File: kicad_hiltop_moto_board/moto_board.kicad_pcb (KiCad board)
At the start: 4 copper layers, 159.9 x 99.9 mm, 213 parts, among them J1 Conn_01x04, J2 Conn_01x04, J3 Conn_03x32_DIN41612, J4 Conn_01x04, J5 Conn_02x05_Top_Bottom, J6 Conn_01x04, J7 Conn_01x04, J8 Conn_01x04, J9 Conn_01x04, Q1 CSD18540Q5B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

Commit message: moto board 3d connector models added
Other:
- board text added: "CH.A"
- board text added: "CH.B"
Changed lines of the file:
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@@
   (general
     (thickness 1.6)
-    (drawings 44)
+    (drawings 48)
     (tracks 1841)
     (zones 0)
@@
     (0 F.Cu signal)
     (1 In1.Cu signal)
-    (2 In2.Cu signal)
+    (2 In2.Cu signal hide)
     (31 B.Cu signal)
     (32 B.Adhes user)
@@
     (pad 1 thru_hole rect (at -5.25 -2.5 270) (size 2.1 2.1) (drill 1.1) (layers *.Cu *.Mask)
       (net 114 /A1))
+    (model /home/adil/Documents/LBBC/KiCAD/kicad_hiltop_moto_board/pxc_1862068_01_SPTAF-1-4-3-5-EL_3D.stp
+      (offset (xyz -7.75 -5.5 0))
+      (scale (xyz 1 1 1))
+      (rotate (xyz 0 0 0))
+    )
   )
   (module Devtank_PCB_Lib:Phoenix_Contact_SPTAF_4_way_terminal_block (layer F.Cu)
@@
     (pad 1 thru_hole rect (at -5.25 -2.5 270) (size 2.1 2.1) (drill 1.1) (layers *.Cu *.Mask)
       (net 111 /B1))
+    (model /home/adil/Documents/LBBC/KiCAD/kicad_hiltop_moto_board/pxc_1862068_01_SPTAF-1-4-3-5-EL_3D.stp
+      (offset (xyz -7.75 -5.5 0))
+      (scale (xyz 1 1 1))
+      (rotate (xyz 0 0 0))
+    )
   )
   (module Resistor_SMD:R_1210_3225Metric (layer F.Cu)
@@
     (tags capacitor)
     (attr smd)
-    (fp_text reference C95 (at -1.96 1.91 180) (layer F.SilkS)
-      (effects (font (size 0.7 0.7) (thickness 0.15)))
+    (fp_text reference C95 (at -1.29 -0.11 270) (layer F.SilkS)
+      (effects (font (size 0.5 0.5) (thickness 0.1)))
     )
     (fp_text value 0.1uF (at 0 1.17 180) (layer F.Fab)
@@
     (tags capacitor)
     (attr smd)
-    (fp_text reference C100 (at -1.285 -1.61 270) (layer F.SilkS)
+    (fp_text reference C100 (at -2.105 0.49) (layer F.SilkS)
       (effects (font (size 0.5 0.5) (thickness 0.1)))
     )
@@
     (pad 7 thru_hole circle (at -12.7 10.16) (size 4.572 4.572) (drill 4.064) (layers *.Cu *.Mask))
     (pad 8 thru_hole circle (at -2.54 10.16) (size 4.572 4.572) (drill 4.064) (layers *.Cu *.Mask))
+    (model /home/adil/Documents/LBBC/KiCAD/kicad_hiltop_moto_board/c-0641737-01-g-3d.stp
+      (offset (xyz -7.5 -12.75 4))
+      (scale (xyz 1 1 1))
+      (rotate (xyz -90 0 0))
+    )
   )
   (module TestPoint:TestPoint_THTPad_D1.0mm_Drill0.5mm (layer F.Cu)
@@
     (descr "Through hole straight pin header, 2x03, 2.54mm pitch, double rows")
     (tags "Through hole pin header THT 2x03 2.54mm double row")
-    (fp_text reference J6 (at -0.96 -2.5) (layer F.SilkS)
+    (fp_text reference J6 (at -2.66 6.4) (layer F.SilkS)
       (effects (font (size 1 1) (thickness 0.15)))
     )
@@
     (descr "Through hole straight pin header, 2x03, 2.54mm pitch, double rows")
     (tags "Through hole pin header THT 2x03 2.54mm double row")
-    (fp_text reference J7 (at -1 -2.5) (layer F.SilkS)
+    (fp_text reference J7 (at -2.66 6.3) (layer F.SilkS)
       (effects (font (size 1 1) (thickness 0.15)))
     )
@@
     (descr "Through hole straight pin header, 2x03, 2.54mm pitch, double rows")
     (tags "Through hole pin header THT 2x03 2.54mm double row")
-    (fp_text reference J8 (at -0.96 -2.5) (layer F.SilkS)
+    (fp_text reference J8 (at -2.66 6) (layer F.SilkS)
       (effects (font (size 1 1) (thickness 0.15)))
     )
@@
     (descr "Through hole straight pin header, 2x03, 2.54mm pitch, double rows")
     (tags "Through hole pin header THT 2x03 2.54mm double row")
-    (fp_text reference J9 (at -1 -2.6) (layer F.SilkS)
+    (fp_text reference J9 (at -2.66 6.3) (layer F.SilkS)
       (effects (font (size 1 1) (thickness 0.15)))
     )
@@
     (pad 1 np_thru_hole circle (at 0 0) (size 2.7 2.7) (drill 2.7) (layers *.Cu *.Mask))
   )
+  (gr_text "CH.B\n" (at 90.9 116.2) (layer F.SilkS)
+    (effects (font (size 0.5 0.5) (thickness 0.1)))
+  )
+  (gr_text "CH.B\n" (at 78.8 116.2) (layer F.SilkS)
+    (effects (font (size 0.5 0.5) (thickness 0.1)))
+  )
+  (gr_text CH.A (at 90.8 105.2) (layer F.SilkS)
+    (effects (font (size 0.5 0.5) (thickness 0.1)))
+  )
+  (gr_text CH.A (at 78.8 105.2) (layer F.SilkS)
+    (effects (font (size 0.5 0.5) (thickness 0.1)))
+  )
   (gr_text "Motor B" (at 196.6 120.1) (layer F.SilkS)

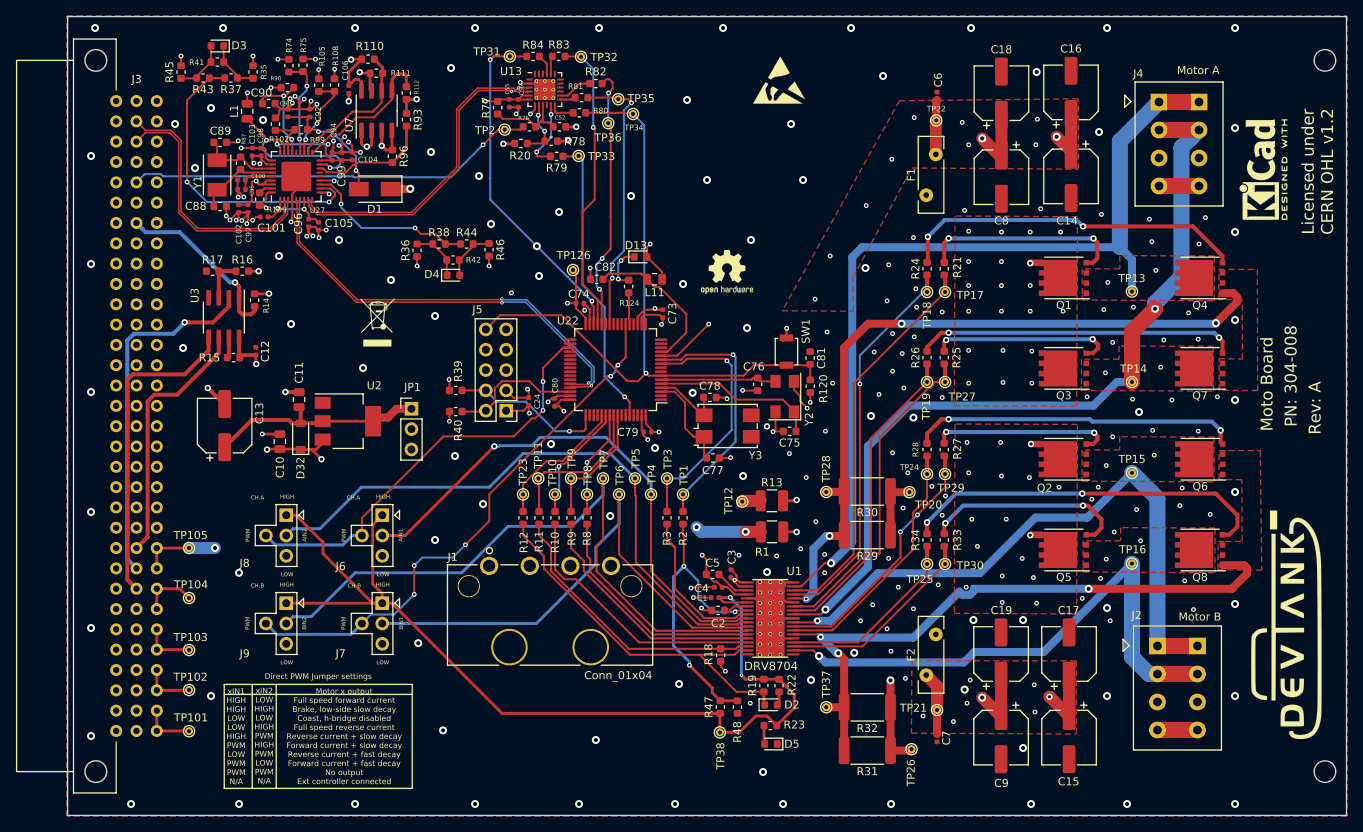
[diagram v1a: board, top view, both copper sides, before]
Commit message: Updated moto board
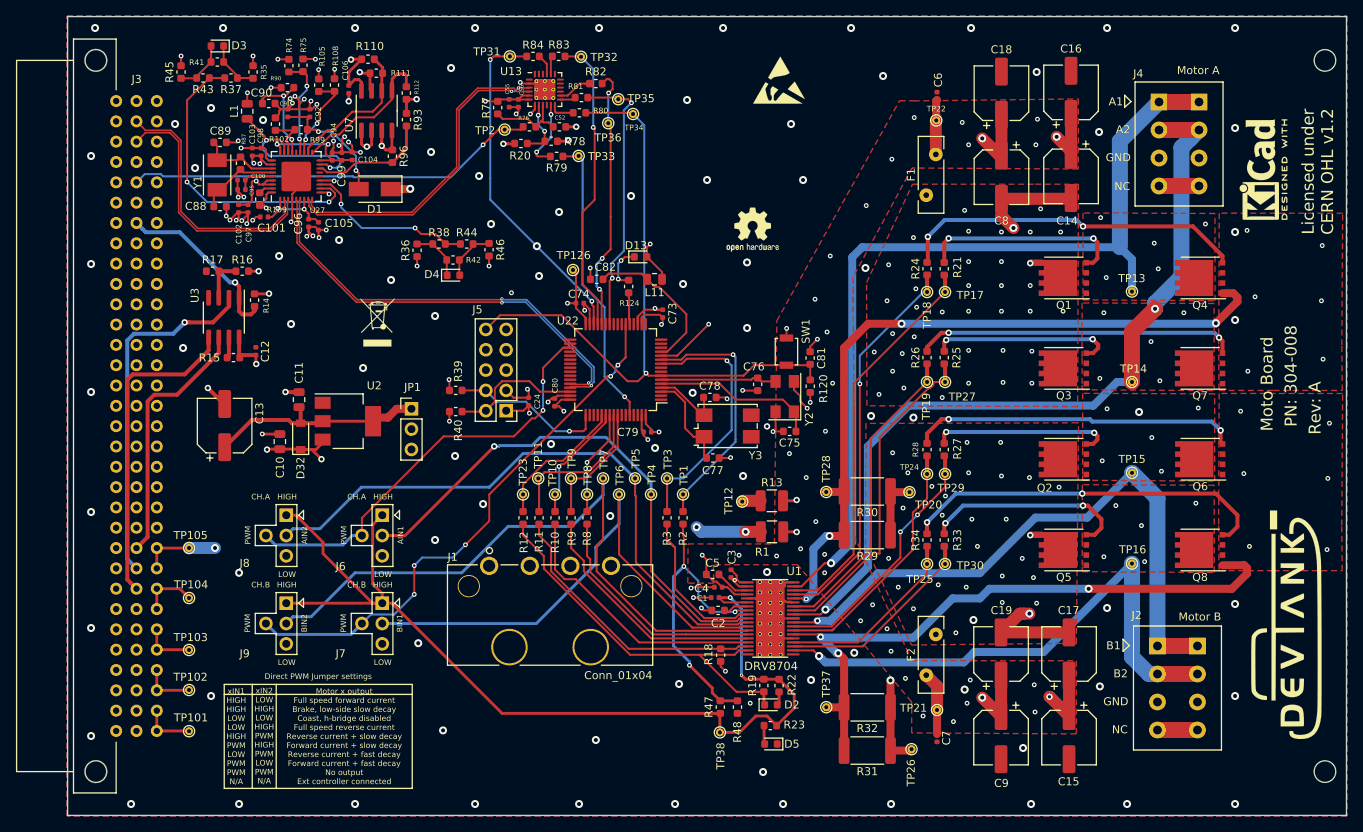
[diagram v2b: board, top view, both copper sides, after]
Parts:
- moved REF** 6.19 mm to (140.7, 71.7)
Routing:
- net GND: track 186.9 -> 214.8 mm
- net Net-(F2-Pad2): track 3.62 -> 2.32 mm, vias 46 -> 27
- net Net-(Q6-Pad1): track 82.5 -> 82.0 mm, vias 3 -> 9
- net Net-(Q4-Pad1): vias 4 -> 10
- net Net-(F1-Pad1): vias 55 -> 36
- net /B2: vias 1 -> 6
- net /B1: vias 1 -> 6
- net /A2: vias 2 -> 7
- net /A1: vias 1 -> 6
- added copper zone on In2.Cu, net /A1
- added copper zone on In2.Cu, net /A2
- added copper zone on In2.Cu, net /B1
- added copper zone on In2.Cu, net /B2
- added copper zone on In2.Cu, net Net-(Q4-Pad1)
- added copper zone on In2.Cu, net Net-(Q6-Pad1)
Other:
- board text added: "A1"
- board text added: "A2"
- board text added: "B1"
- board text added: "B2"
- board text added: "GND"
- board text added: "NC"

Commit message: Moto board csd mosfet footprint changes
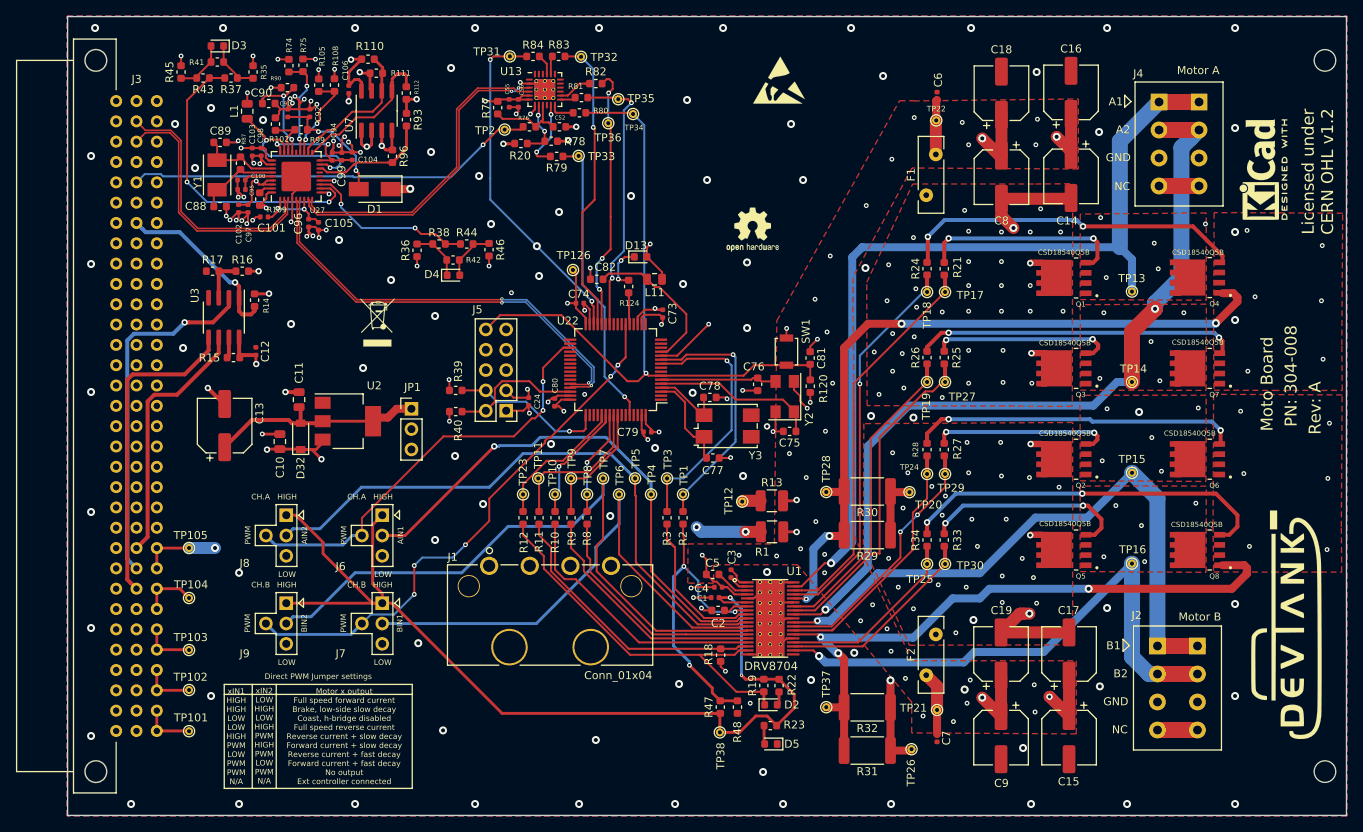
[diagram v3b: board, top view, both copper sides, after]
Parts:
- Q1, Q2, Q3, Q4, Q5, Q6, Q7, Q8: footprint Devtank_PCB_Lib:CSD18540Q5B -> Devtank_PCB_Lib:TI_CSD18540Q5B
- moved Q6 0.35 mm to (196.3, 100.4)
- moved Q4 0.33 mm to (196.3, 77.7)
- moved Q7 0.33 mm to (196.3, 89.0)
- moved Q8 0.33 mm to (196.3, 111.8)
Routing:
- net GND: track 214.8 -> 204.5 mm, vias 154 -> 155
- net Net-(F2-Pad2): track 2.32 -> 3.67 mm, vias 27 -> 28
- net Net-(F1-Pad1): track 3.16 -> 4.41 mm

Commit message: Moto Board Rev A
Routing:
- net GND: track 204.5 -> 204.9 mm, vias 155 -> 157
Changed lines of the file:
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@@
     (thickness 1.6)
     (drawings 56)
-    (tracks 1837)
+    (tracks 1842)
     (zones 0)
     (modules 213)
@@
   )
   (setup
-    (last_trace_width 0.25)
+    (last_trace_width 1.5)
     (user_trace_width 0.2)
     (user_trace_width 0.25)
@@
       (effects (font (size 1.03766 1.03766) (thickness 0.05)))
     )
-    (fp_text value DRV8704 (at 0.1 5.97304) (layer F.SilkS)
+    (fp_text value DRV8704 (at 0.1 5.97304) (layer F.SilkS) hide
       (effects (font (size 1.04569 1.04569) (thickness 0.05)))
     )
@@
     (pad 1 smd rect (at -2.87 -4.5) (size 1.57 0.28) (layers F.Cu F.Paste F.Mask)
       (net 65 "Net-(C3-Pad1)"))
+    (model /home/adil/Documents/LBBC/KiCAD/kicad_hiltop_moto_board/DRV8704.stp
+      (at (xyz 0 0 0))
+      (scale (xyz 1 1 1))
+      (rotate (xyz 0 0 0))
+    )
   )
   (module Devtank_PCB_Lib:Phoenix_Contact_SPTAF_4_way_terminal_block (layer F.Cu)
@@
     (pad 1 thru_hole rect (at -5.25 -2.5 270) (size 2.1 2.1) (drill 1.1) (layers *.Cu *.Mask)
       (net 114 /A1))
+    (model /home/adil/Documents/LBBC/KiCAD/kicad_hiltop_moto_board/pxc_1862068_01_SPTAF-1-4-3-5-EL_3D.stp
+      (offset (xyz -7.75 -5.5 0))
+      (scale (xyz 1 1 1))
+      (rotate (xyz 0 0 0))
+    )
   )
   (module Devtank_PCB_Lib:Phoenix_Contact_SPTAF_4_way_terminal_block (layer F.Cu)
@@
     (pad 1 thru_hole rect (at -5.25 -2.5 270) (size 2.1 2.1) (drill 1.1) (layers *.Cu *.Mask)
       (net 111 /B1))
+    (model /home/adil/Documents/LBBC/KiCAD/kicad_hiltop_moto_board/pxc_1862068_01_SPTAF-1-4-3-5-EL_3D.stp
+      (offset (xyz -7.75 -5.5 0))
+      (scale (xyz 1 1 1))
+      (rotate (xyz 0 0 0))
+    )
   )
   (module Resistor_SMD:R_1210_3225Metric (layer F.Cu)
@@
       (effects (font (size 1 1) (thickness 0.15)))
     )
-    (fp_text value Conn_01x04 (at 0.9 13.7) (layer F.SilkS)
+    (fp_text value Conn_01x04 (at 0.9 13.7) (layer F.SilkS) hide
       (effects (font (size 1 1) (thickness 0.15)))
     )
@@
     (pad 7 thru_hole circle (at -12.7 10.16) (size 4.572 4.572) (drill 4.064) (layers *.Cu *.Mask))
     (pad 8 thru_hole circle (at -2.54 10.16) (size 4.572 4.572) (drill 4.064) (layers *.Cu *.Mask))
+    (model /home/adil/Documents/LBBC/KiCAD/kicad_hiltop_moto_board/c-0641737-01-g-3d.stp
+      (offset (xyz -7.75 -12.75 4))
+      (scale (xyz 1 1 1))
+      (rotate (xyz -90 0 0))
+    )
   )
   (module TestPoint:TestPoint_THTPad_D1.0mm_Drill0.5mm (layer F.Cu)
@@
       (effects (font (size 0.64 0.64) (thickness 0.05)))
     )
-    (fp_text value CSD18540Q5B (at 0 3.2036) (layer F.SilkS)
+    (fp_text value CSD18540Q5B (at 0 3.2036) (layer F.SilkS) hide
       (effects (font (size 0.64 0.64) (thickness 0.05)))
     )
@@
       (effects (font (size 0.64 0.64) (thickness 0.05)))
     )
-    (fp_text value CSD18540Q5B (at -0.14 3.235) (layer F.SilkS)
+    (fp_text value CSD18540Q5B (at -0.14 3.235) (layer F.SilkS) hide
       (effects (font (size 0.64 0.64) (thickness 0.05)))
     )
@@
     (pad 3 smd rect (at 2.77 1.905) (size 1.372 0.71) (layers F.Cu F.Paste F.Mask)
       (net 92 "Net-(F2-Pad2)"))
+    (model /home/adil/Documents/LBBC/KiCAD/kicad_hiltop_moto_board/CSD18540Q5B.stp
+      (at (xyz 0 0 0))
+      (scale (xyz 1 1 1))
+      (rotate (xyz 0 0 0))
+    )
   )
   (module Devtank_PCB_Lib:TI_CSD18540Q5B (layer F.Cu)
@@
       (effects (font (size 0.64 0.64) (thickness 0.05)))
     )
-    (fp_text value CSD18540Q5B (at -0.14 3.18) (layer F.SilkS)
+    (fp_text value CSD18540Q5B (at -0.14 3.18) (layer F.SilkS) hide
       (effects (font (size 0.64 0.64) (thickness 0.05)))
     )
@@
     (pad 3 smd rect (at 2.77 1.905) (size 1.372 0.71) (layers F.Cu F.Paste F.Mask)
       (net 30 "Net-(F1-Pad1)"))
+    (model /home/adil/Documents/LBBC/KiCAD/kicad_hiltop_moto_board/CSD18540Q5B.stp
+      (at (xyz 0 0 0))
+      (scale (xyz 1 1 1))
+      (rotate (xyz 0 0 0))
+    )
   )
   (module Devtank_PCB_Lib:TI_CSD18540Q5B (layer F.Cu)
@@
       (effects (font (size 0.64 0.64) (thickness 0.05)))
     )
-    (fp_text value CSD18540Q5B (at -0.07 3.15) (layer F.SilkS)
+    (fp_text value CSD18540Q5B (at -0.07 3.15) (layer F.SilkS) hide
       (effects (font (size 0.64 0.64) (thickness 0.05)))
     )
@@
     (pad 3 smd rect (at 0.93 0.01 180) (size 3.85 4.52) (layers F.Cu F.Paste F.Mask)
       (net 114 /A1))
+    (model /home/adil/Documents/LBBC/KiCAD/kicad_hiltop_moto_board/CSD18540Q5B.stp
+      (at (xyz 0 0 0))
+      (scale (xyz 1 1 1))
+      (rotate (xyz 0 0 0))
+    )
   )
   (module Devtank_PCB_Lib:TI_CSD18540Q5B (layer F.Cu)
@@
       (effects (font (size 0.64 0.64) (thickness 0.05)))
     )
-    (fp_text value CSD18540Q5B (at -0.16 3.28) (layer F.SilkS)
+    (fp_text value CSD18540Q5B (at -0.16 3.28) (layer F.SilkS) hide
       (effects (font (size 0.64 0.64) (thickness 0.05)))
     )
@@
     (pad 3 smd rect (at 0.93 0.01 180) (size 3.85 4.52) (layers F.Cu F.Paste F.Mask)
       (net 92 "Net-(F2-Pad2)"))
+    (model /home/adil/Documents/LBBC/KiCAD/kicad_hiltop_moto_board/CSD18540Q5B.stp
+      (at (xyz 0 0 0))
+      (scale (xyz 1 1 1))
+      (rotate (xyz 0 0 0))
+    )
   )
   (module Devtank_PCB_Lib:TI_CSD18540Q5B (layer F.Cu)
@@
       (effects (font (size 0.64 0.64) (thickness 0.05)))
     )
-    (fp_text value CSD18540Q5B (at 0.95 3.245) (layer F.SilkS)
+    (fp_text value CSD18540Q5B (at 0.95 3.245) (layer F.SilkS) hide
       (effects (font (size 0.64 0.64) (thickness 0.05)))
     )
@@
     (pad 3 smd rect (at 0.93 0.01 180) (size 3.85 4.52) (layers F.Cu F.Paste F.Mask)
       (net 111 /B1))
+    (model /home/adil/Documents/LBBC/KiCAD/kicad_hiltop_moto_board/CSD18540Q5B.stp
+      (at (xyz 0 0 0))
+      (scale (xyz 1 1 1))
+      (rotate (xyz 0 0 0))
+    )
   )
   (module Devtank_PCB_Lib:TI_CSD18540Q5B (layer F.Cu)
@@
       (effects (font (size 0.64 0.64) (thickness 0.05)))
     )
-    (fp_text value CSD18540Q5B (at -0.04 3.26) (layer F.SilkS)
+    (fp_text value CSD18540Q5B (at -0.04 3.26) (layer F.SilkS) hide
       (effects (font (size 0.64 0.64) (thickness 0.05)))
     )
@@
     (pad 3 smd rect (at 0.93 0.01 180) (size 3.85 4.52) (layers F.Cu F.Paste F.Mask)
       (net 113 /A2))
+    (model /home/adil/Documents/LBBC/KiCAD/kicad_hiltop_moto_board/CSD18540Q5B.stp
+      (at (xyz 0 0 0))
+      (scale (xyz 1 1 1))
+      (rotate (xyz 0 0 0))
+    )
   )
   (module Devtank_PCB_Lib:TI_CSD18540Q5B (layer F.Cu)
@@
       (effects (font (size 0.64 0.64) (thickness 0.05)))
     )
-    (fp_text value CSD18540Q5B (at 0.07 3.18) (layer F.SilkS)
+    (fp_text value CSD18540Q5B (at 0.07 3.18) (layer F.SilkS) hide
       (effects (font (size 0.64 0.64) (thickness 0.05)))
     )
@@
     (pad 3 smd rect (at 2.77 1.905) (size 1.372 0.71) (layers F.Cu F.Paste F.Mask)
       (net 112 /B2))
+    (model /home/adil/Documents/LBBC/KiCAD/kicad_hiltop_moto_board/CSD18540Q5B.stp
+      (at (xyz 0 0 0))
+      (scale (xyz 1 1 1))
+      (rotate (xyz 0 0 0))
+    )
   )
   (gr_text B1 (at 185.8 123.7) (layer F.SilkS)
@@
   (segment (start 180.4 67.85) (end 180.5 67.75) (width 1.5) (layer F.Cu) (net 1) (status 30))
   (segment (start 171.8 67.85) (end 180.4 67.85) (width 1.5) (layer F.Cu) (net 1) (status 30))
-  (via (at 173.3 71.5) (size 1) (drill 0.5) (layers F.Cu B.Cu) (net 1))
-  (segment (start 171.8 67.85) (end 171.8 70) (width 1.5) (layer F.Cu) (net 1) (status 10))
-  (segment (start 171.8 70) (end 173.3 71.5) (width 1.5) (layer F.Cu) (net 1))
   (segment (start 171.75 122.05) (end 180.25 122.05) (width 1.5) (layer F.Cu) (net 1) (status 30))
-  (via (at 175.300006 119.7) (size 1) (drill 0.5) (layers F.Cu B.Cu) (net 1))
-  (segment (start 171.75 122.05) (end 174.1 119.7) (width 1.5) (layer F.Cu) (net 1) (status 10))
-  (segment (start 174.5929 119.7) (end 175.300006 119.7) (width 1.5) (layer F.Cu) (net 1))
-  (segment (start 174.1 119.7) (end 174.5929 119.7) (width 1.5) (layer F.Cu) (net 1))
   (via (at 148.8 85.4) (size 0.6) (drill 0.3) (layers F.Cu B.Cu) (net 1))
   (segment (start 147.885 86.9625) (end 147.885 86.315) (width 0.25) (layer F.Cu) (net 1) (status 10))
@@
   (segment (start 141.55 124.8) (end 141.6 124.85) (width 0.25) (layer F.Cu) (net 1) (status 30))
   (segment (start 140.03 124.8) (end 141.55 124.8) (width 0.25) (layer F.Cu) (net 1) (status 30))
+  (via (at 170.07 121.98) (size 1) (drill 0.5) (layers F.Cu B.Cu) (net 1))
+  (segment (start 171.75 122.05) (end 170.14 122.05) (width 1.5) (layer F.Cu) (net 1))
+  (segment (start 170.14 122.05) (end 170.07 121.98) (width 1.5) (layer F.Cu) (net 1))
+  (via (at 183.28 122.03) (size 1) (drill 0.5) (layers F.Cu B.Cu) (net 1))
+  (segment (start 180.25 122.05) (end 183.26 122.05) (width 1.5) (layer F.Cu) (net 1))
+  (segment (start 183.26 122.05) (end 183.28 122.03) (width 1.5) (layer F.Cu) (net 1))
+  (via (at 169.96 67.9) (size 1) (drill 0.5) (layers F.Cu B.Cu) (net 1))
+  (segment (start 171.8 67.85) (end 170.01 67.85) (width 1.5) (layer F.Cu) (net 1))
+  (segment (start 170.01 67.85) (end 169.96 67.9) (width 1.5) (layer F.Cu) (net 1))
+  (via (at 183.1 67.8) (size 1) (drill 0.5) (layers F.Cu B.Cu) (net 1))
+  (segment (start 180.5 67.75) (end 183.05 67.75) (width 1.5) (layer F.Cu) (net 1))
+  (segment (start 183.05 67.75) (end 183.1 67.8) (width 1.5) (layer F.Cu) (net 1))
   (segment (start 127.199299 81.715) (end 126.324999 82.5893) (width 0.25) (layer F.Cu) (net 2))
   (segment (start 126.324999 82.654999) (end 126.324999 83.529999) (width 0.25) (layer F.Cu) (net 2) (status 20))
